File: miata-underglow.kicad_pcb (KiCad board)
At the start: 2 copper layers, 73 x 70 mm, 34 parts, among them J1 Micro_SD_Card, J2 FTDI, J3 LEDS, J4 CAN, Q1 SS8050, Q2 SS8050, U1 AMS1117-3.3, U2 TXS0108EPW, U3 AMS1117-5.0, U4 ESP32-WROOM-32D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

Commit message: Progress on routing
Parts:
- R7: footprint Resistor_SMD:R_0402_1005Metric -> Resistor_SMD:R_1206_3216Metric
- moved H4 146.9 mm to (170.8, 80.7)
- moved C9 73.1 mm to (48.8, 93.6), turned to 90 degrees
- moved JP1 69.2 mm to (68.2, 94.7), turned to 0 degrees
- moved C1 68.4 mm to (23.9, 93.6), turned to 0 degrees
- moved J4 66.7 mm to (68.5, 101.8), turned to 0 degrees
- moved J2 66.2 mm to (112.3, 62.8)
- moved C5 63.7 mm to (35.4, 20.2)
- moved R7 61.9 mm to (72.2, 94.7)
- moved J3 60.8 mm to (34.5, 101.8), turned to 0 degrees
- moved D2 59.8 mm to (27.7, 48.1), turned to 90 degrees
- moved U5 59.0 mm to (45.3, 86.9), turned to 270 degrees
- moved R3 57.3 mm to (29.4, 45.0), turned to 270 degrees
- moved D1 56.9 mm to (29.4, 48.1), turned to 90 degrees
- moved R4 56.7 mm to (27.7, 45.0), turned to 270 degrees
- moved C2 56.5 mm to (32.9, 95.8), turned to 0 degrees
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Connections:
- J1 pad 1: (no net) -> /SD_D2
- J1 pad 8: (no net) -> /SD_D1
- J2 pad 2: (no net) -> /FTDI_CTS
- J2 pad 3: (no net) -> /FTDI_VCC
- J3 pad 10: /LED2_OUT -> /LED0_OUT
- J3 pad 11: /LED3_OUT -> /LED1_OUT
- J3 pad 2: (no net) -> +12V
- J3 pad 3: (no net) -> +12V
- J3 pad 4: (no net) -> +12V
- J3 pad 5: (no net) -> GND
- J3 pad 6: (no net) -> GND
- J3 pad 7: (no net) -> GND
- J3 pad 8: /LED0_OUT -> /LED3_OUT
- J3 pad 9: /LED1_OUT -> /LED2_OUT
- Q1 pad 2: (no net) -> /RESET
- Q2 pad 2: (no net) -> /GPIO0
- U2 pad 1: /LED0 -> GND
- U2 pad 10: (no net) -> +3V3
- U2 pad 12: (no net) -> GND
- U2 pad 13: (no net) -> GND
- U2 pad 14: (no net) -> GND
- U2 pad 15: (no net) -> /LED3_OUT
- U2 pad 16: /LED3_OUT -> /LED2_OUT
- U2 pad 17: /LED2_OUT -> /LED0_OUT
- U2 pad 20: /LED0_OUT -> GND
- U2 pad 4: /LED2 -> /LED0
- U2 pad 5: /LED3 -> /LED2
- U2 pad 6: (no net) -> /LED3
- U2 pad 7: (no net) -> GND
- U2 pad 8: (no net) -> GND
- U2 pad 9: (no net) -> GND
- U4 pad 10: /LED0 -> /CAN_TX2_RTS
- U4 pad 11: /LED1 -> /CAN_TX1_RTS
- U4 pad 12: /LED2 -> /CAN_TX0_RTS
- U4 pad 13: /CAN_TX0_RTS -> /LED2
- U4 pad 14: /CAN_TX2_RTS -> /LED1
- U4 pad 16: /CAN_TX1_RTS -> /LED0
- U4 pad 17: (no net) -> Net-(U4-Pad17)
- U4 pad 18: (no net) -> Net-(U4-Pad18)
- U4 pad 19: (no net) -> Net-(U4-Pad19)
- U4 pad 20: (no net) -> Net-(U4-Pad20)
- U4 pad 21: (no net) -> Net-(U4-Pad21)
- U4 pad 22: (no net) -> Net-(U4-Pad22)
- U4 pad 23: /CAN_RX1_BF -> /LED3
- U4 pad 25: (no net) -> Net-(U4-Pad25)
- U4 pad 3: (no net) -> Net-(U4-Pad3)
- U4 pad 32: (no net) -> Net-(U4-Pad32)
- U4 pad 4: (no net) -> Net-(U4-Pad4)
- U4 pad 5: (no net) -> Net-(U4-Pad5)
- U4 pad 6: (no net) -> Net-(U4-Pad6)
- U4 pad 7: (no net) -> Net-(U4-Pad7)
- U4 pad 8: /LED3 -> /CAN_RX1_BF
- U5 pad 2: (no net) -> Net-(U5-Pad2)
- U5 pad 22: (no net) -> Net-(U5-Pad22)
- U5 pad 25: (no net) -> Net-(U5-Pad25)
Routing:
- net /SD_D0: track 0.00 -> 70.6 mm
- net /SPI_CS: track 0.00 -> 63.6 mm
- net GND: track 0.00 -> 57.1 mm, vias 0 -> 4
- net /CANL: track 0.00 -> 51.3 mm, vias 0 -> 1
- net /CANH: track 0.00 -> 47.0 mm, vias 0 -> 1
- net /SD_CMD: track 0.00 -> 37.5 mm, vias 0 -> 2
- net /CAN_RX0_BF: track 0.00 -> 36.7 mm
- net /CAN_INT: track 0.00 -> 36.4 mm
- net /SD_CLK: track 0.00 -> 35.0 mm
- net /LED3: track 0.00 -> 34.1 mm
- net +3V3: track 0.00 -> 32.4 mm, vias 0 -> 3
- net /LED0: track 0.00 -> 22.1 mm
- net /CAN_TX0_RTS: track 0.00 -> 20.1 mm
- net /LED3_OUT: track 0.00 -> 18.2 mm
- net +5V: track 0.00 -> 16.7 mm, vias 0 -> 2
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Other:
- board outline removed

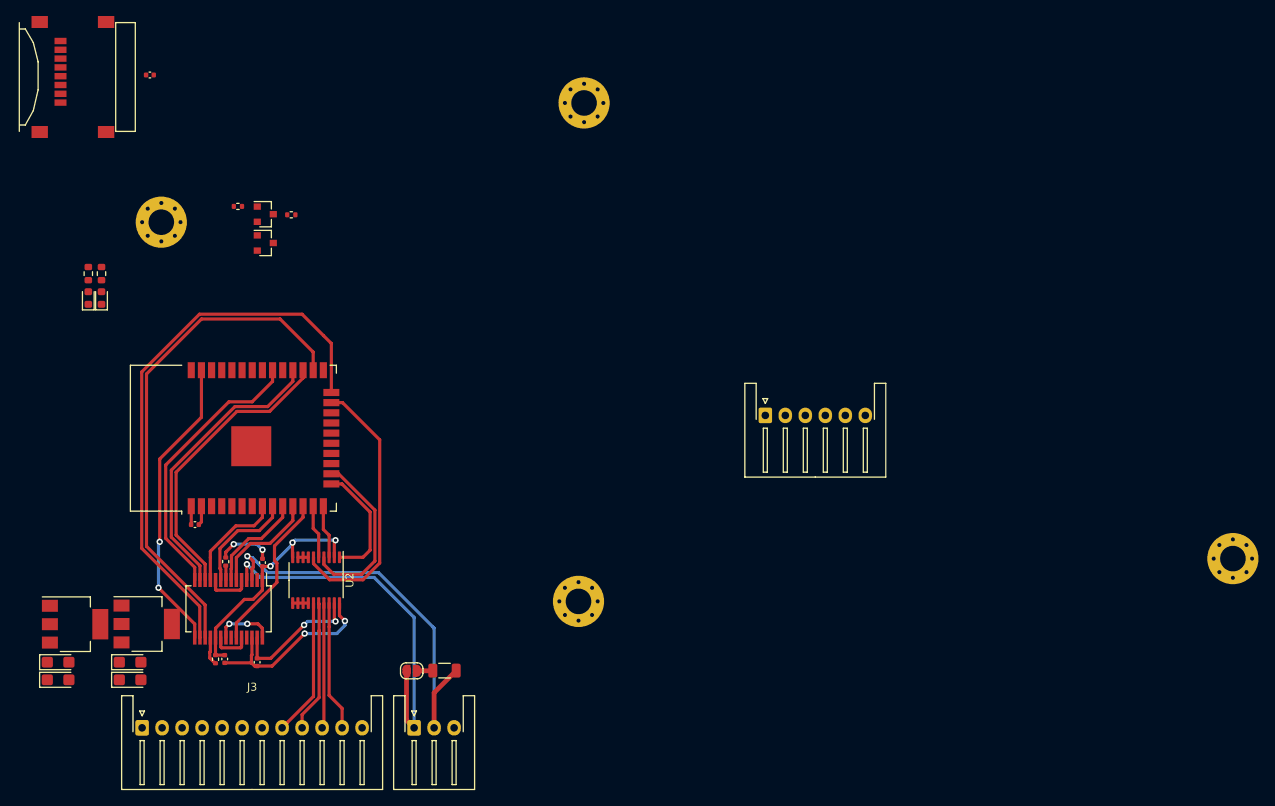
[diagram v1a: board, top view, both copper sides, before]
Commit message: More routing progress
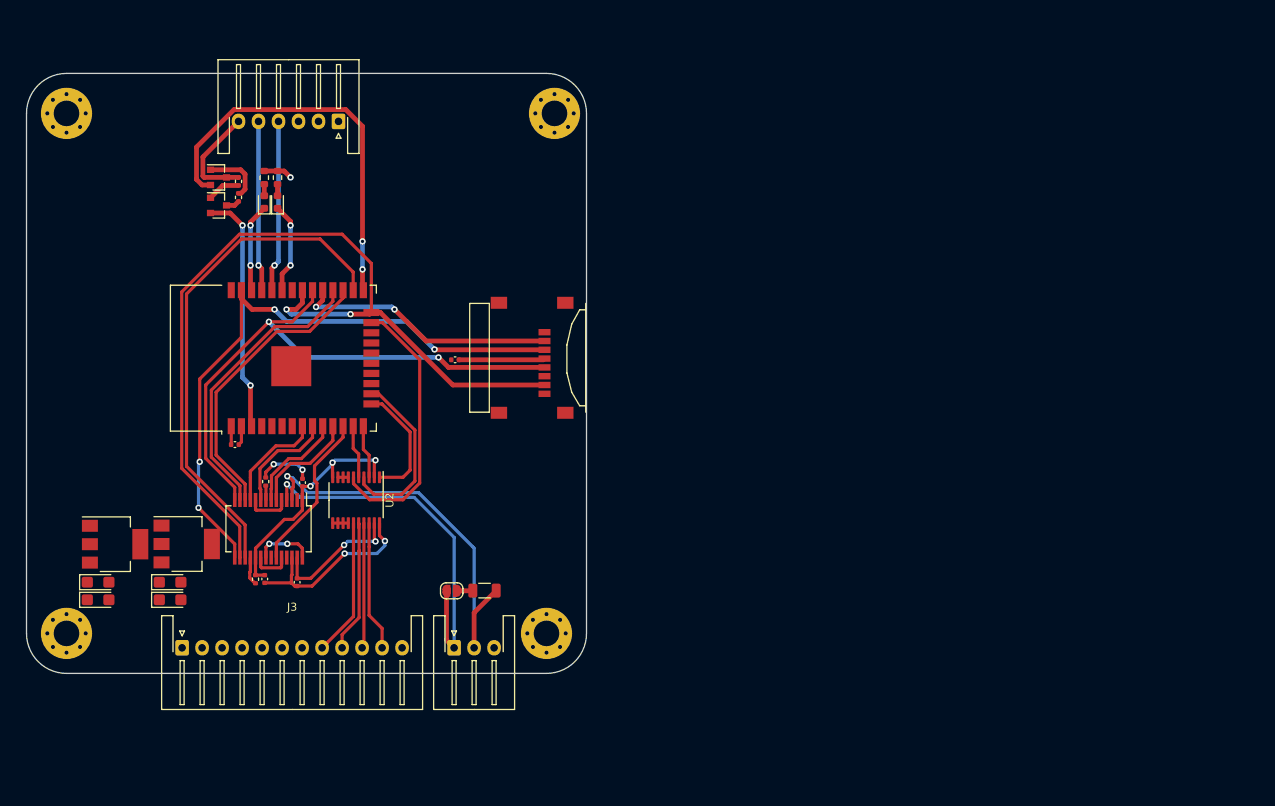
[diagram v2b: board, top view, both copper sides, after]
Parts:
- moved H4 86.3 mm to (85.0, 90.0)
- moved J1 66.3 mm to (82.7, 55.5), turned to 90 degrees
- moved J2 64.8 mm to (59.0, 26.0), turned to 180 degrees
- moved H3 64.1 mm to (25.0, 90.0)
- moved C5 52.2 mm to (73.6, 55.8)
- moved D1 25.1 mm to (51.4, 36.1)
- moved R3 25.1 mm to (51.4, 33.0)
- moved R4 25.1 mm to (49.7, 33.0)
- moved D2 25.1 mm to (49.7, 36.1)
- moved H1 18.0 mm to (25.0, 25.0)
- moved C1 11.2 mm to (28.9, 83.6)
- moved C2 11.2 mm to (37.9, 85.8)
- moved C3 11.2 mm to (38.0, 83.6)
- moved C4 11.2 mm to (28.9, 85.8)
- moved C6 11.2 mm to (46.1, 66.4)
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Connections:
- J1 pad 1: /SD_D2 -> (no net)
- J1 pad 8: /SD_D1 -> (no net)
- J2 pad 2: /FTDI_CTS -> (no net)
- J2 pad 3: /FTDI_VCC -> (no net)
- U4 pad 17: Net-(U4-Pad17) -> (no net)
- U4 pad 18: Net-(U4-Pad18) -> (no net)
- U4 pad 19: Net-(U4-Pad19) -> (no net)
- U4 pad 20: Net-(U4-Pad20) -> (no net)
- U4 pad 21: Net-(U4-Pad21) -> (no net)
- U4 pad 22: Net-(U4-Pad22) -> (no net)
- U4 pad 25: Net-(U4-Pad25) -> /GPIO0
- U4 pad 3: Net-(U4-Pad3) -> /RESET
- U4 pad 32: Net-(U4-Pad32) -> (no net)
- U4 pad 4: Net-(U4-Pad4) -> (no net)
- U4 pad 5: Net-(U4-Pad5) -> (no net)
- U4 pad 6: Net-(U4-Pad6) -> (no net)
- U4 pad 7: Net-(U4-Pad7) -> (no net)
- U5 pad 2: Net-(U5-Pad2) -> (no net)
- U5 pad 22: Net-(U5-Pad22) -> (no net)
- U5 pad 25: Net-(U5-Pad25) -> (no net)
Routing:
- net /GPIO0: track 0.00 -> 50.2 mm, vias 0 -> 2
- net /SD_CMD: track 37.5 -> 79.1 mm, vias 2 -> 4
- net /SD_D0: track 70.6 -> 110.8 mm, vias 0 -> 2
- net /SD_CLK: track 35.0 -> 71.8 mm, vias 0 -> 2
- net /SD_D3: track 0.00 -> 32.8 mm, vias 0 -> 2
- net /RESET: track 0.00 -> 30.2 mm, vias 0 -> 2
- net /FTDI_TX: track 0.00 -> 21.4 mm, vias 0 -> 1
- net /FTDI_RX: track 0.00 -> 21.3 mm, vias 0 -> 1
- net +3V3: track 32.4 -> 46.8 mm, vias 3 -> 4
- net /FTDI_DTR: track 0.00 -> 13.2 mm
- net /STATUS0: track 0.00 -> 11.3 mm, vias 0 -> 2
- net /STATUS1: track 0.00 -> 11.0 mm, vias 0 -> 2
- net Net-(Q2-Pad1): track 0.00 -> 7.47 mm
- net Net-(Q1-Pad1): track 0.00 -> 4.14 mm
- net /FTDI_RTS: track 0.00 -> 1.70 mm
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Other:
- board outline added: 70 x 75 mm

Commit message: p much complete i think
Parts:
- moved C4 15.0 mm to (42.5, 79.2), turned to 270 degrees
- moved C1 13.5 mm to (42.5, 83.8), turned to 90 degrees
- moved U1 12.2 mm to (28.1, 81.7), turned to 90 degrees
- moved C2 8.39 mm to (32.9, 79.1), turned to 270 degrees
- moved U3 7.24 mm to (37.7, 81.7), turned to 90 degrees
- moved C3 5.05 mm to (32.9, 83.8), turned to 90 degrees
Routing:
- net GND: track 57.1 -> 112.8 mm, vias 4 -> 16
- net +12V: track 0.00 -> 26.0 mm
- net +5V: track 16.7 -> 36.3 mm, vias 2 -> 4
- net +3V3: track 46.8 -> 63.7 mm, vias 4 -> 9
- added copper zone on B.Cu, net +12V
- added copper zone on F.Cu, net +12V
- added copper zone on F.Cu, net +3V3
- added copper zone on In1.Cu, net +3V3
- added copper zone on F.Cu, net +5V
- added copper zone on B.Cu, net GND
- added copper zone on F.Cu, net GND
- added copper zone on In2.Cu, net GND
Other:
- copper layers 2 -> 4
